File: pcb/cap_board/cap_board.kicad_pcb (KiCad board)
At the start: 2 copper layers, 78.7 x 54.6 mm, 12 parts, among them J1 Conn_01x02, J2 Conn_01x02, J3 Conn_01x02, J4 Conn_01x02, J5 Conn_01x02, J6 Conn_01x02, J7 RJ45, J8 RJ45, U1 Adafruit_MPR121

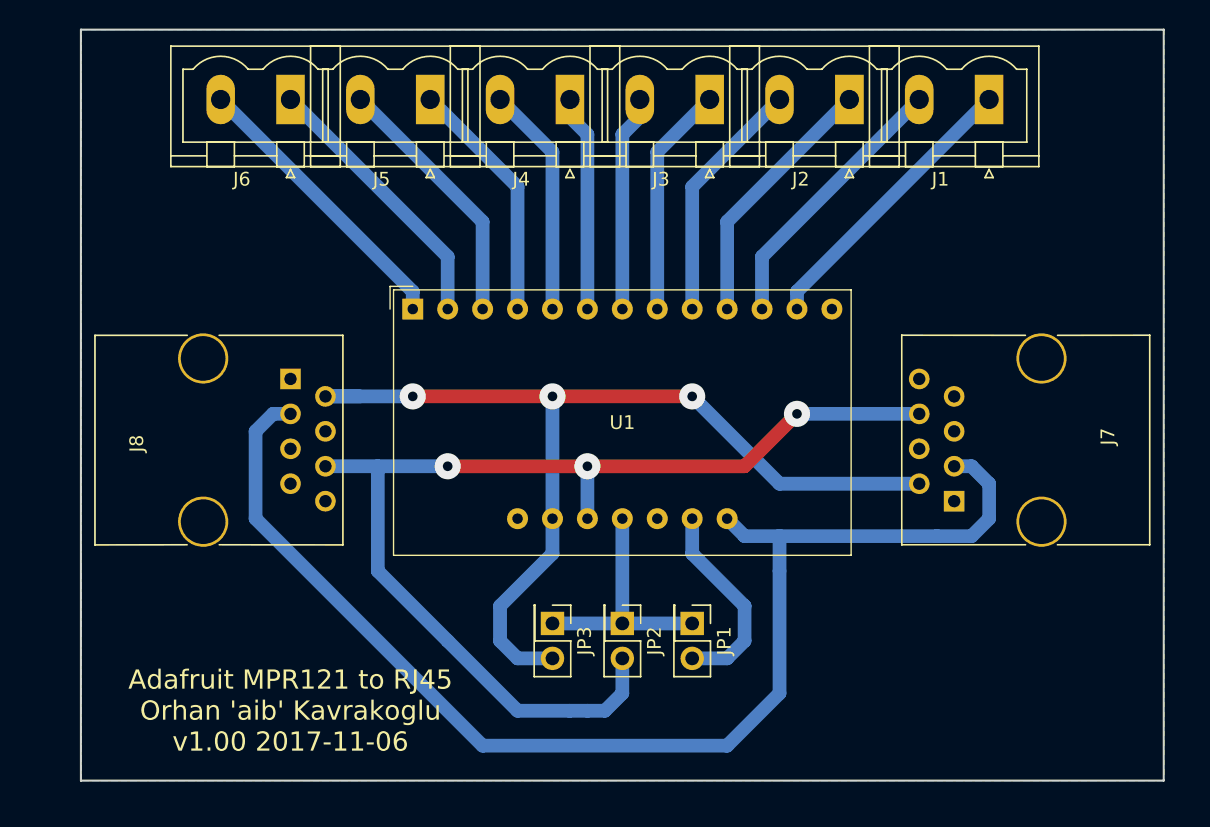
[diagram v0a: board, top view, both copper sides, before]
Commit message: Add mounting holes and round the board
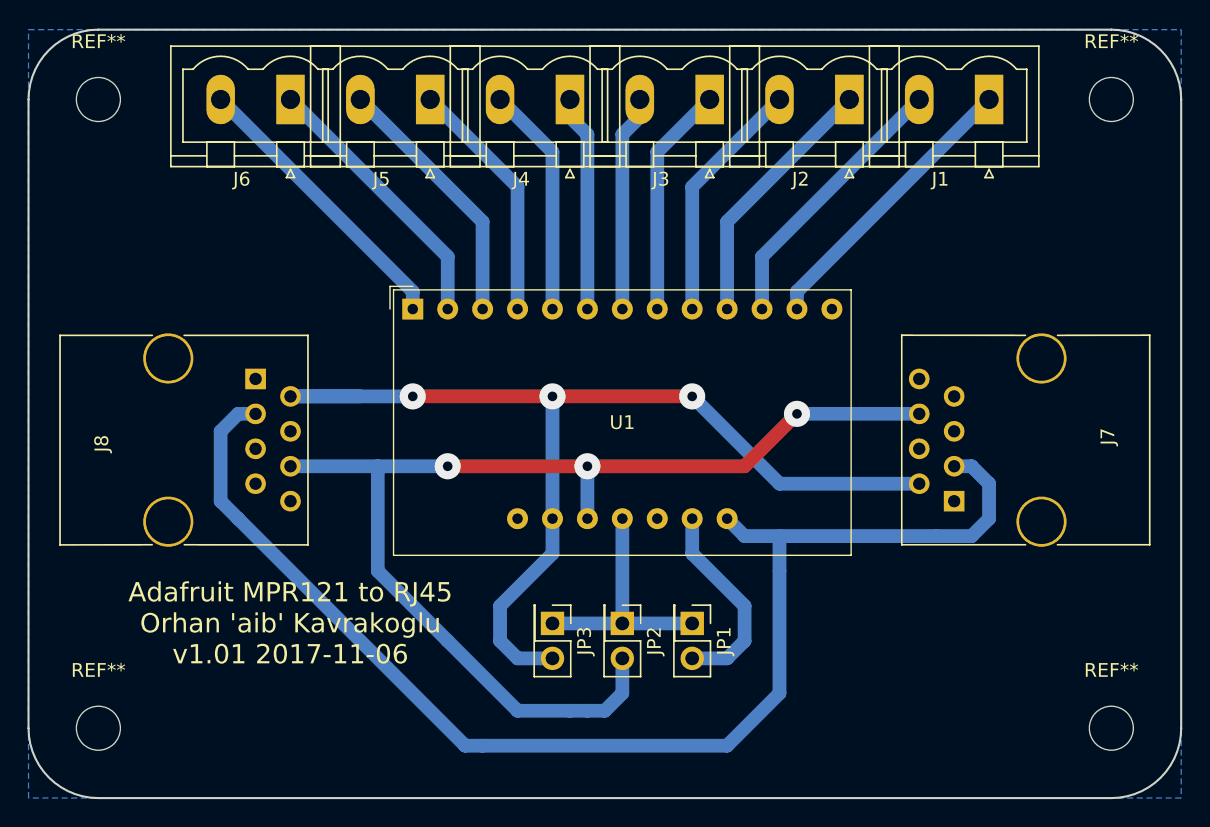
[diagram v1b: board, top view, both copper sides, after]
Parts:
- added REF**: MountingHole_3.2mm_M3, Mounting_Holes:MountingHole_3.2mm_M3, F.Cu at (129.5, 127.0)
- added REF**: MountingHole_3.2mm_M3, Mounting_Holes:MountingHole_3.2mm_M3, F.Cu at (55.9, 81.3)
- added REF**: MountingHole_3.2mm_M3, Mounting_Holes:MountingHole_3.2mm_M3, F.Cu at (129.5, 81.3)
- added REF**: MountingHole_3.2mm_M3, Mounting_Holes:MountingHole_3.2mm_M3, F.Cu at (55.9, 127.0)
- moved J8 2.54 mm to (67.3, 101.6)
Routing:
- net /SCL: track 72.0 -> 77.1 mm
- net /SDA: track 81.2 -> 83.8 mm
- net +5V: track 93.1 -> 94.9 mm
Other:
- board size 78.7 x 54.6 mm -> 83.8 x 55.9 mm
- board text added: "Adafruit MPR121 to RJ45 Orhan 'aib' Kavrakoglu v1.01 2017-11-06"
- board text removed: "Adafruit MPR121 to RJ45 Orhan 'aib' Kavrakoglu v1.00 2017-11-06"

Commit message: Add front plate zone
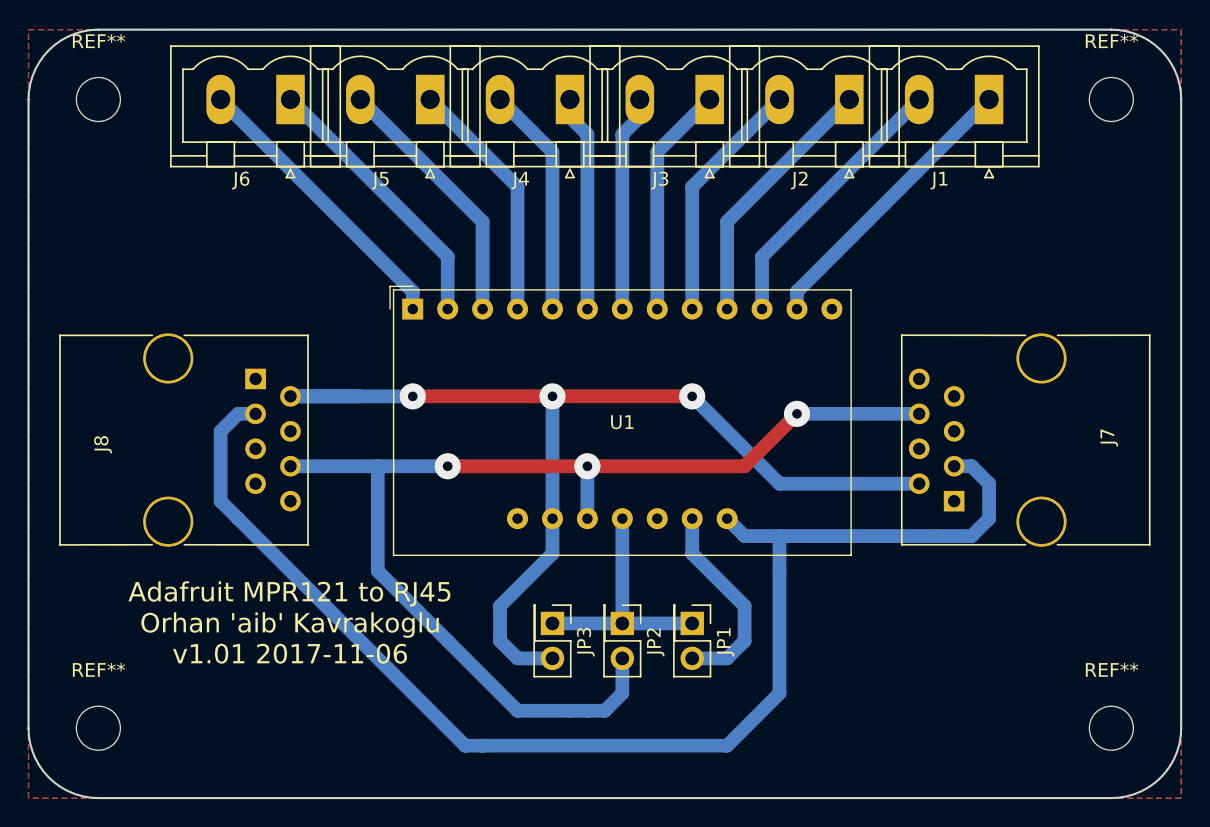
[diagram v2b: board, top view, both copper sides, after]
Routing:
- added copper zone on F.Cu, net +5V
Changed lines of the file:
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@@
     (links 27)
     (no_connects 0)
-    (area 45.922857 75.105 139.497143 132.675)
+    (area 45.922857 75.105 146.28 138.590001)
     (thickness 1.6)
     (drawings 11)
@@
   (segment (start 85.09 120.65) (end 85.09 118.11) (width 1) (layer B.Cu) (net 14))
   (segment (start 86.36 121.92) (end 85.09 120.65) (width 1) (layer B.Cu) (net 14))
+  (segment (start 119.38 107.95) (end 120.65 109.22) (width 1) (layer B.Cu) (net 15))
+  (segment (start 119.38 107.95) (end 118.11 107.95) (width 1) (layer B.Cu) (net 15))
+  (segment (start 120.65 109.22) (end 120.65 111.76) (width 1) (layer B.Cu) (net 15))
+  (segment (start 120.65 111.76) (end 119.38 113.03) (width 1) (layer B.Cu) (net 15))
+  (segment (start 116.84 113.03) (end 105.41 113.03) (width 1) (layer B.Cu) (net 15))
+  (segment (start 119.38 113.03) (end 116.84 113.03) (width 1) (layer B.Cu) (net 15))
   (segment (start 66.04 111.76) (end 82.55 128.27) (width 1) (layer B.Cu) (net 15))
+  (segment (start 105.41 113.03) (end 102.87 113.03) (width 1) (layer B.Cu) (net 15))
+  (segment (start 102.87 113.03) (end 101.6 111.76) (width 1) (layer B.Cu) (net 15))
+  (segment (start 66.04 111.76) (end 64.77 110.49) (width 1) (layer B.Cu) (net 15))
+  (segment (start 64.77 110.49) (end 64.77 105.41) (width 1) (layer B.Cu) (net 15))
+  (segment (start 64.77 105.41) (end 66.04 104.14) (width 1) (layer B.Cu) (net 15))
+  (segment (start 66.04 104.14) (end 67.31 104.14) (width 1) (layer B.Cu) (net 15))
+  (segment (start 105.41 124.46) (end 101.6 128.27) (width 1) (layer B.Cu) (net 15))
+  (segment (start 101.6 128.27) (end 83.82 128.27) (width 1) (layer B.Cu) (net 15))
+  (segment (start 105.41 113.03) (end 105.41 115.57) (width 1) (layer B.Cu) (net 15))
+  (segment (start 105.41 115.57) (end 105.41 124.46) (width 1) (layer B.Cu) (net 15))
   (segment (start 82.55 128.27) (end 83.82 128.27) (width 1) (layer B.Cu) (net 15))
-  (segment (start 105.41 115.57) (end 105.41 124.46) (width 1) (layer B.Cu) (net 15))
-  (segment (start 105.41 113.03) (end 105.41 115.57) (width 1) (layer B.Cu) (net 15))
-  (segment (start 101.6 128.27) (end 83.82 128.27) (width 1) (layer B.Cu) (net 15))
-  (segment (start 105.41 124.46) (end 101.6 128.27) (width 1) (layer B.Cu) (net 15))
-  (segment (start 66.04 104.14) (end 67.31 104.14) (width 1) (layer B.Cu) (net 15))
-  (segment (start 64.77 105.41) (end 66.04 104.14) (width 1) (layer B.Cu) (net 15))
-  (segment (start 64.77 110.49) (end 64.77 105.41) (width 1) (layer B.Cu) (net 15))
-  (segment (start 66.04 111.76) (end 64.77 110.49) (width 1) (layer B.Cu) (net 15))
-  (segment (start 119.38 107.95) (end 120.65 109.22) (width 1) (layer B.Cu) (net 15))
-  (segment (start 119.38 113.03) (end 116.84 113.03) (width 1) (layer B.Cu) (net 15))
-  (segment (start 116.84 113.03) (end 105.41 113.03) (width 1) (layer B.Cu) (net 15))
-  (segment (start 120.65 111.76) (end 119.38 113.03) (width 1) (layer B.Cu) (net 15))
-  (segment (start 120.65 109.22) (end 120.65 111.76) (width 1) (layer B.Cu) (net 15))
-  (segment (start 119.38 107.95) (end 118.11 107.95) (width 1) (layer B.Cu) (net 15))
-  (segment (start 102.87 113.03) (end 101.6 111.76) (width 1) (layer B.Cu) (net 15))
-  (segment (start 105.41 113.03) (end 102.87 113.03) (width 1) (layer B.Cu) (net 15))
   (segment (start 76.2 107.95) (end 76.2 115.57) (width 1) (layer B.Cu) (net 18))
   (segment (start 76.2 115.57) (end 81.28 120.65) (width 1) (layer B.Cu) (net 18))
@@
     (connect_pads yes (clearance 0.7))
     (min_thickness 1)
+    (fill yes (arc_segments 16) (thermal_gap 0.7) (thermal_bridge_width 0.7))
+    (polygon
+      (pts
+        (xy 134.62 76.2) (xy 134.62 132.08) (xy 50.8 132.08) (xy 50.8 76.2)
+      )
+    )
+  )
+  (zone (net 15) (net_name +5V) (layer F.Cu) (hatch edge 0.508)
+    (connect_pads yes (clearance 0.7))
+    (min_thickness 1)

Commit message: Change +5V to VCC
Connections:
- net +5V renamed VCC

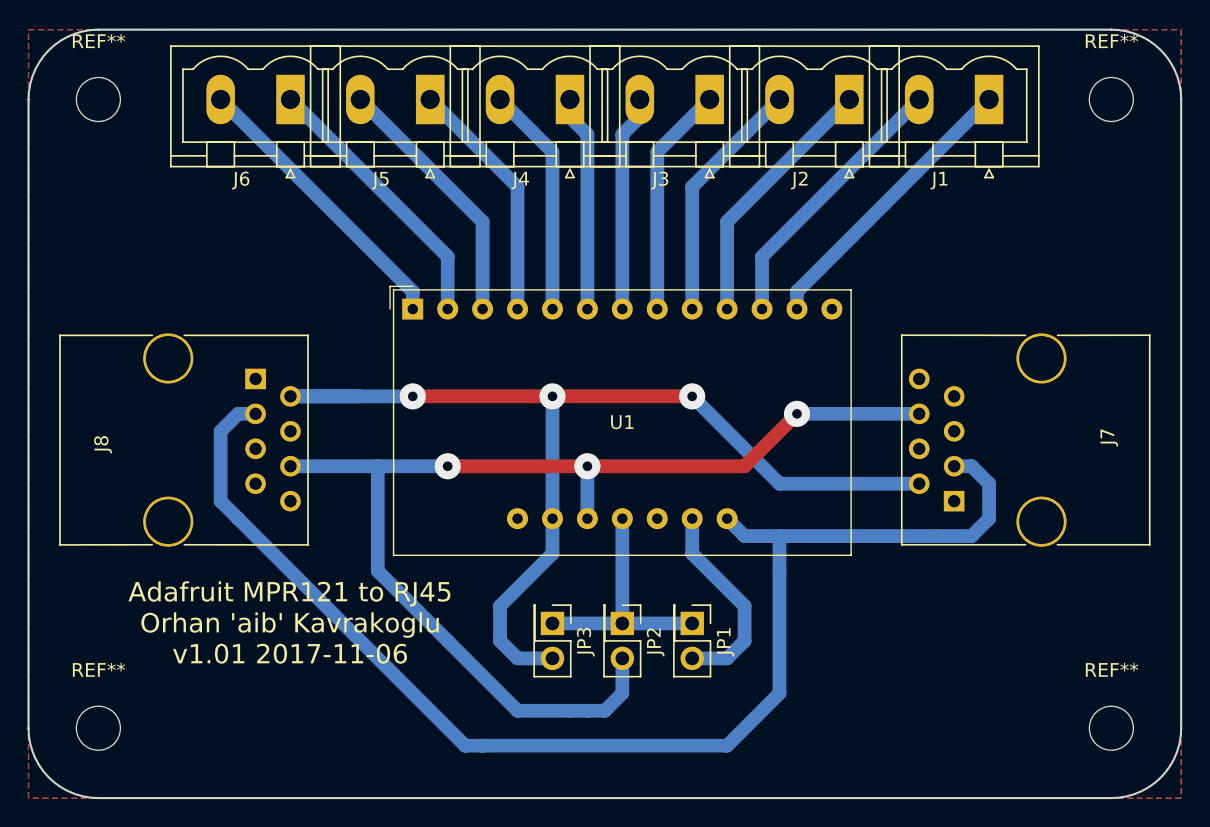
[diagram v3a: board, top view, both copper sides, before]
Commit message: Use a 12-pin connector and add silkscreen text
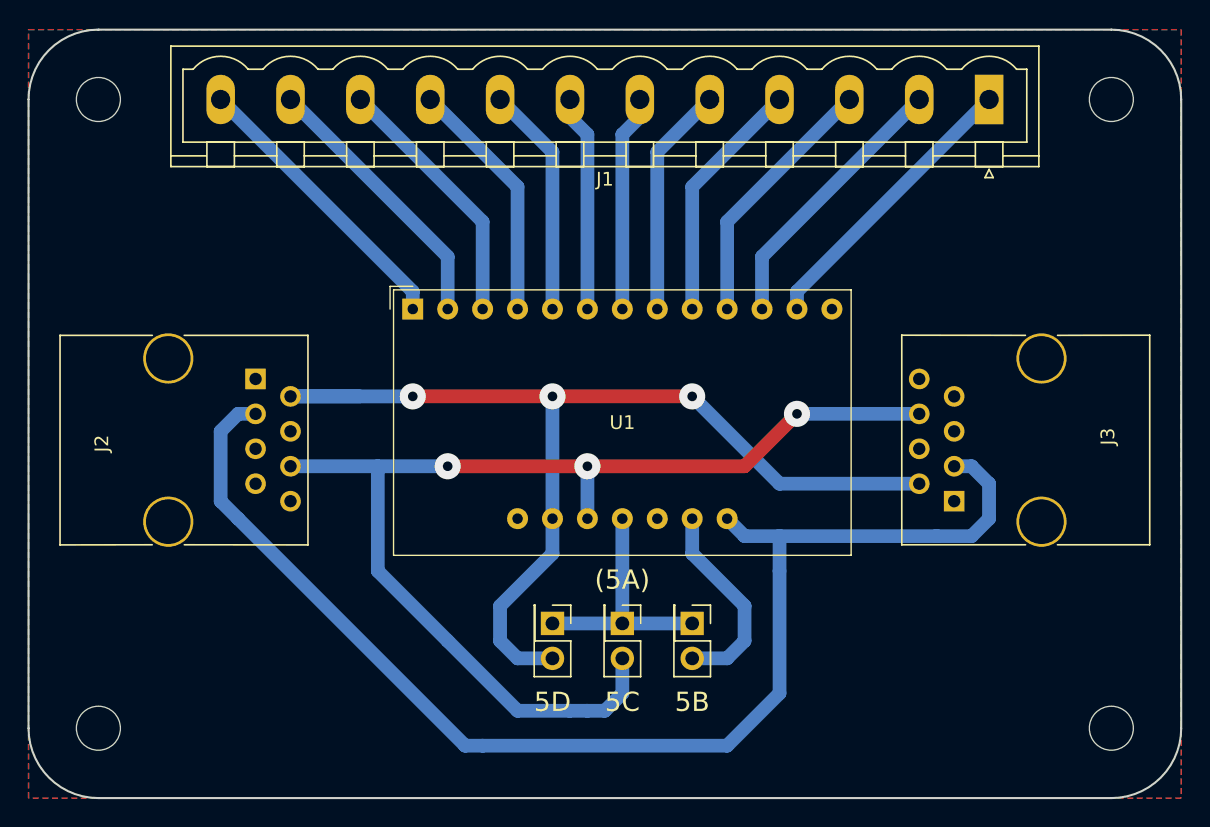
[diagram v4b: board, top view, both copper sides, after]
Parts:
- removed J4, J5, J6: Conn_01x02, Connectors_Phoenix:PhoenixContact_MSTBVA-G_02x5.08mm_Vertical
- removed J7, J8: RJ45, Connectors:RJ45_8
- J1: value Conn_01x02 -> Conn_01x12; footprint Connectors_Phoenix:PhoenixContact_MSTBVA-G_02x5.08mm_Vertical -> Connectors_Phoenix:PhoenixContact_MSTBVA-G_12x5.08mm_Vertical
- J2, J3: value Conn_01x02 -> RJ45; footprint Connectors_Phoenix:PhoenixContact_MSTBVA-G_02x5.08mm_Vertical -> Connectors:RJ45_8
- moved J2 47.7 mm to (67.3, 101.6), turned to 270 degrees
- moved J3 34.2 mm to (118.1, 110.5), turned to 90 degrees
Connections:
- J2 pad 1: Net-(J2-Pad1) -> GND
- J2 pad 2: Net-(J2-Pad2) -> /SCL
- J3 pad 1: Net-(J3-Pad1) -> GND
- J3 pad 2: Net-(J3-Pad2) -> /SCL
- U1 pad 11: Net-(J2-Pad1) -> Net-(J1-Pad3)
- U1 pad 12: Net-(J2-Pad2) -> Net-(J1-Pad4)
- U1 pad 13: Net-(J3-Pad1) -> Net-(J1-Pad5)
- U1 pad 14: Net-(J3-Pad2) -> Net-(J1-Pad6)
- U1 pad 15: Net-(J4-Pad1) -> Net-(J1-Pad7)
- U1 pad 16: Net-(J4-Pad2) -> Net-(J1-Pad8)
- U1 pad 17: Net-(J5-Pad1) -> Net-(J1-Pad9)
- U1 pad 18: Net-(J5-Pad2) -> Net-(J1-Pad10)
- U1 pad 19: Net-(J6-Pad1) -> Net-(J1-Pad11)
- U1 pad 20: Net-(J6-Pad2) -> Net-(J1-Pad12)
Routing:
- net Net-(J6-Pad2): track 22.3 -> 0.00 mm
- net Net-(J1-Pad12): track 0.00 -> 22.3 mm
- net Net-(J6-Pad1): track 21.2 -> 0.00 mm
- net Net-(J1-Pad11): track 0.00 -> 21.2 mm
- net Net-(J2-Pad1): track 18.9 -> 0.00 mm
- net Net-(J1-Pad3): track 0.00 -> 18.9 mm
- net Net-(J5-Pad2): track 18.9 -> 0.00 mm
- net Net-(J1-Pad10): track 0.00 -> 18.9 mm
- net Net-(J5-Pad1): track 17.9 -> 0.00 mm
- net Net-(J2-Pad2): track 17.9 -> 0.00 mm
- net Net-(J1-Pad9): track 0.00 -> 17.9 mm
- net Net-(J1-Pad4): track 0.00 -> 17.9 mm
- net Net-(J4-Pad2): track 16.8 -> 0.00 mm
- net Net-(J3-Pad1): track 16.8 -> 0.00 mm
- net Net-(J1-Pad8): track 0.00 -> 16.8 mm
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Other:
- board text added: "(5A)"
- board text added: "5B"
- board text added: "5C"
- board text added: "5D"
- board text added: "Adafruit MPR121 to RJ45 Orhan 'aib' Kavrakoglu 2017-11-06"
- board text added: "v1.02 20171109"
- board text removed: "Adafruit MPR121 to RJ45 Orhan 'aib' Kavrakoglu v1.01 2017-11-06"
